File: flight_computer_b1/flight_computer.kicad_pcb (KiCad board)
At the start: 4 copper layers, 78 x 67 mm, 77 parts, among them J1 Pi Connector, J2 Conn_02x02_Odd_Even, J3 Conn_01x03, J4 DB25_Socket, J5 DB25_Socket, U1 IRLML6344TRPBF, U2 IRLML6344TRPBF, U3 IRLML6344TRPBF, U4 IRLML6344TRPBF, U5 LMR51430XDDCR, U6 ADS1158IRTCR, U7 MIC94161YCS-TR, U8 MCP6001-OT, U9 MCP6001-OT, Y1 32.768kHz

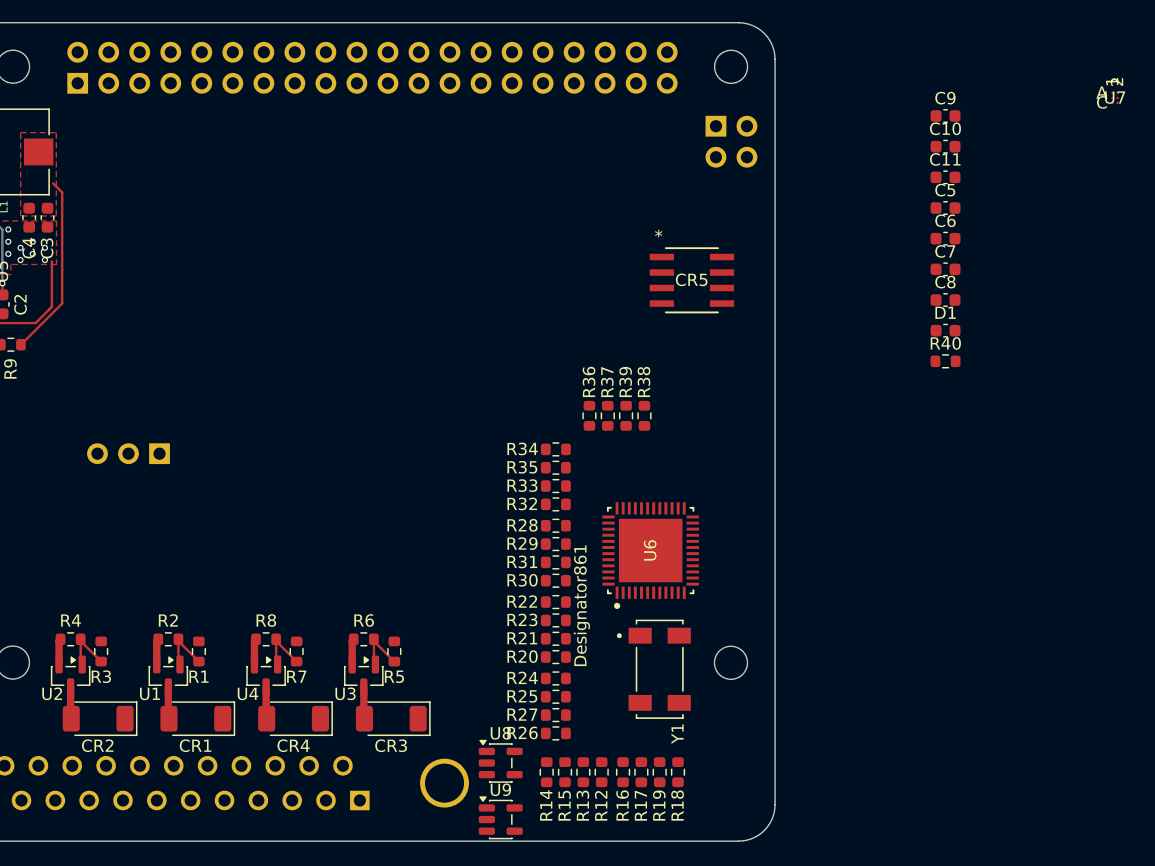
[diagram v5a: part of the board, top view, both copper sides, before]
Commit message: flight computer: added mux and voltage sense channels
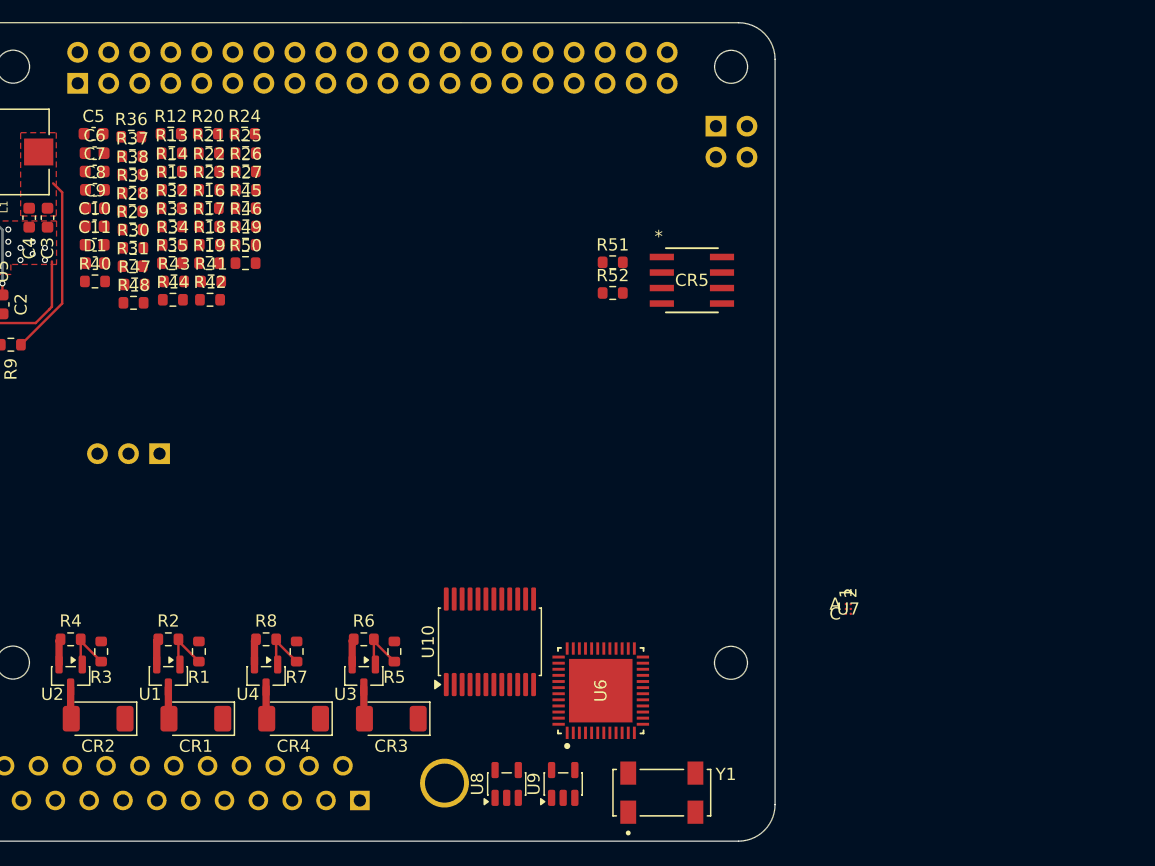
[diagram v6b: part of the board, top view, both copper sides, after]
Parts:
- added R41: 4k, Resistor_SMD:R_0603_1608Metric, F.Cu at (134.3, 92.5)
- added R42: 1k, Resistor_SMD:R_0603_1608Metric, F.Cu at (134.2, 94.0)
- added R43: 4k, Resistor_SMD:R_0603_1608Metric, F.Cu at (131.3, 92.5)
- added R44: 1k, Resistor_SMD:R_0603_1608Metric, F.Cu at (131.2, 94.0)
- added R45: 4k, Resistor_SMD:R_0603_1608Metric, F.Cu at (137.1, 86.5)
- added R46: 1k, Resistor_SMD:R_0603_1608Metric, F.Cu at (137.2, 88.0)
- added R47: 4k, Resistor_SMD:R_0603_1608Metric, F.Cu at (128.1, 92.8)
- added R48: 1k, Resistor_SMD:R_0603_1608Metric, F.Cu at (128.0, 94.3)
- added R49: 4k, Resistor_SMD:R_0603_1608Metric, F.Cu at (137.1, 89.5)
- added R50: 1k, Resistor_SMD:R_0603_1608Metric, F.Cu at (137.1, 91.0)
- added R51: 1k, Resistor_SMD:R_0603_1608Metric, F.Cu at (167.2, 90.9)
- added R52: 1k, Resistor_SMD:R_0603_1608Metric, F.Cu at (167.2, 93.5)
- added U10: CD74HC4067SM, Package_SO:SSOP-24_5.3x8.2mm_P0.65mm, F.Cu at (157.1, 122.0)
- moved C8 70.2 mm to (124.8, 85.0)
- moved C7 70.1 mm to (124.8, 83.5)
- moved C9 70.0 mm to (124.8, 86.5)
- moved C6 70.0 mm to (124.8, 82.0)
- moved C5 70.0 mm to (124.7, 80.4)
- moved C10 70.0 mm to (124.8, 88.0)
- moved R40 69.9 mm to (124.8, 92.5)
- moved C11 69.9 mm to (124.8, 89.5)
- moved D1 69.8 mm to (124.8, 91.0)
- moved R12 63.1 mm to (131.0, 80.4), turned to 0 degrees
- moved R13 60.9 mm to (131.1, 82.0), turned to 0 degrees
- moved R14 58.0 mm to (131.1, 83.5), turned to 0 degrees
- moved R18 57.7 mm to (134.2, 89.5), turned to 0 degrees
- moved R15 57.5 mm to (131.1, 85.0), turned to 0 degrees
- moved R16 57.3 mm to (134.1, 86.5), turned to 0 degrees
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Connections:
- net /pt_div0/INPUT+ renamed /PT_0+
- net /pt_div0/INPUT- renamed /PT_0-
- net /pt_div1/INPUT+ renamed /PT_1+
- net /pt_div1/INPUT- renamed /PT_1-
- net /pt_div2/INPUT+ renamed /PT_2+
- net /pt_div2/INPUT- renamed /PT_2-
- net /pt_div3/INPUT+ renamed /PT_3+
- net /pt_div3/INPUT- renamed /PT_3-
- net /pt_div4/INPUT+ renamed /PT_4+
- net /pt_div4/INPUT- renamed /PT_4-
- net /pt_div5/INPUT+ renamed /PT_5+
- net /pt_div5/INPUT- renamed /PT_5-
- net /pt_div6/INPUT+ renamed /PT_6+
- net /pt_div6/INPUT- renamed /PT_6-
- C3 pad 1: +5V -> /24_5_buck/5V
- C4 pad 1: +5V -> /24_5_buck/5V
- CR5 pad 1: +5V_ISO -> +5V
- J1 pad 2: +5V_ISO -> +5V
- J1 pad 29: unconnected-(J1-Pin_29-Pad29) -> /valve3_enable
- J1 pad 3: unconnected-(J1-Pin_3-Pad3) -> /valve0_enable
- J1 pad 4: +5V_ISO -> +5V
- J1 pad 5: unconnected-(J1-Pin_5-Pad5) -> /valve1_enable
- J1 pad 7: unconnected-(J1-Pin_7-Pad7) -> /valve2_enable
- L1 pad 2: +5V -> /24_5_buck/5V
- R1 pad 1: /valve0/ENABLE -> /valve0_enable
- R3 pad 1: /valve1/ENABLE -> /valve1_enable
- R5 pad 1: /valve2/ENABLE -> /valve2_enable
- R7 pad 1: /valve3/ENABLE -> /valve3_enable
- R9 pad 1: +5V -> /24_5_buck/5V
- U1 pad 1: Net-(U1-G) -> /valve0_excitation_return
- U1 pad 2: GND -> Net-(U1-G)
- U1 pad 3: /valve0_excitation_return -> GND
- U2 pad 1: Net-(U2-G) -> /valve1_excitation_return
- U2 pad 2: GND -> Net-(U2-G)
- U2 pad 3: /valve1_excitation_return -> GND
- U3 pad 1: Net-(U3-G) -> /valve2_excitation_return
- U3 pad 2: GND -> Net-(U3-G)
- U3 pad 3: /valve2_excitation_return -> GND
- U4 pad 1: Net-(U4-G) -> /valve3_excitation_return
- U4 pad 2: GND -> Net-(U4-G)
- U4 pad 3: /valve3_excitation_return -> GND
- U6 pad 10: +5V_ISO -> +5V
- U6 pad 11: +5V_ISO -> +5V
- U6 pad 26: +5V_ISO -> +5V
- U7 pad A1: +5V_ISO -> +5V
- U7 pad A2: +5V -> /24_5_buck/5V
- U7 pad B1: +5V_ISO -> +5V
- U7 pad B2: +5V -> /24_5_buck/5V
- U7 pad C2: +5V -> /24_5_buck/5V
- U8 pad 5: +5V_ISO -> +5V
- U9 pad 5: +5V_ISO -> +5V
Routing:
- net /24_5_buck/5V: track 0.00 -> 14.9 mm
- net +5V: track 14.9 -> 0.00 mm
- net Net-(U2-G): track 4.63 -> 0.00 mm
- net /valve1_excitation_return: track 2.58 -> 7.22 mm
- net Net-(U4-G): track 4.63 -> 0.00 mm
- net Net-(U3-G): track 4.63 -> 0.00 mm
- net /valve3_excitation_return: track 2.58 -> 7.22 mm
- net /valve2_excitation_return: track 2.58 -> 7.22 mm

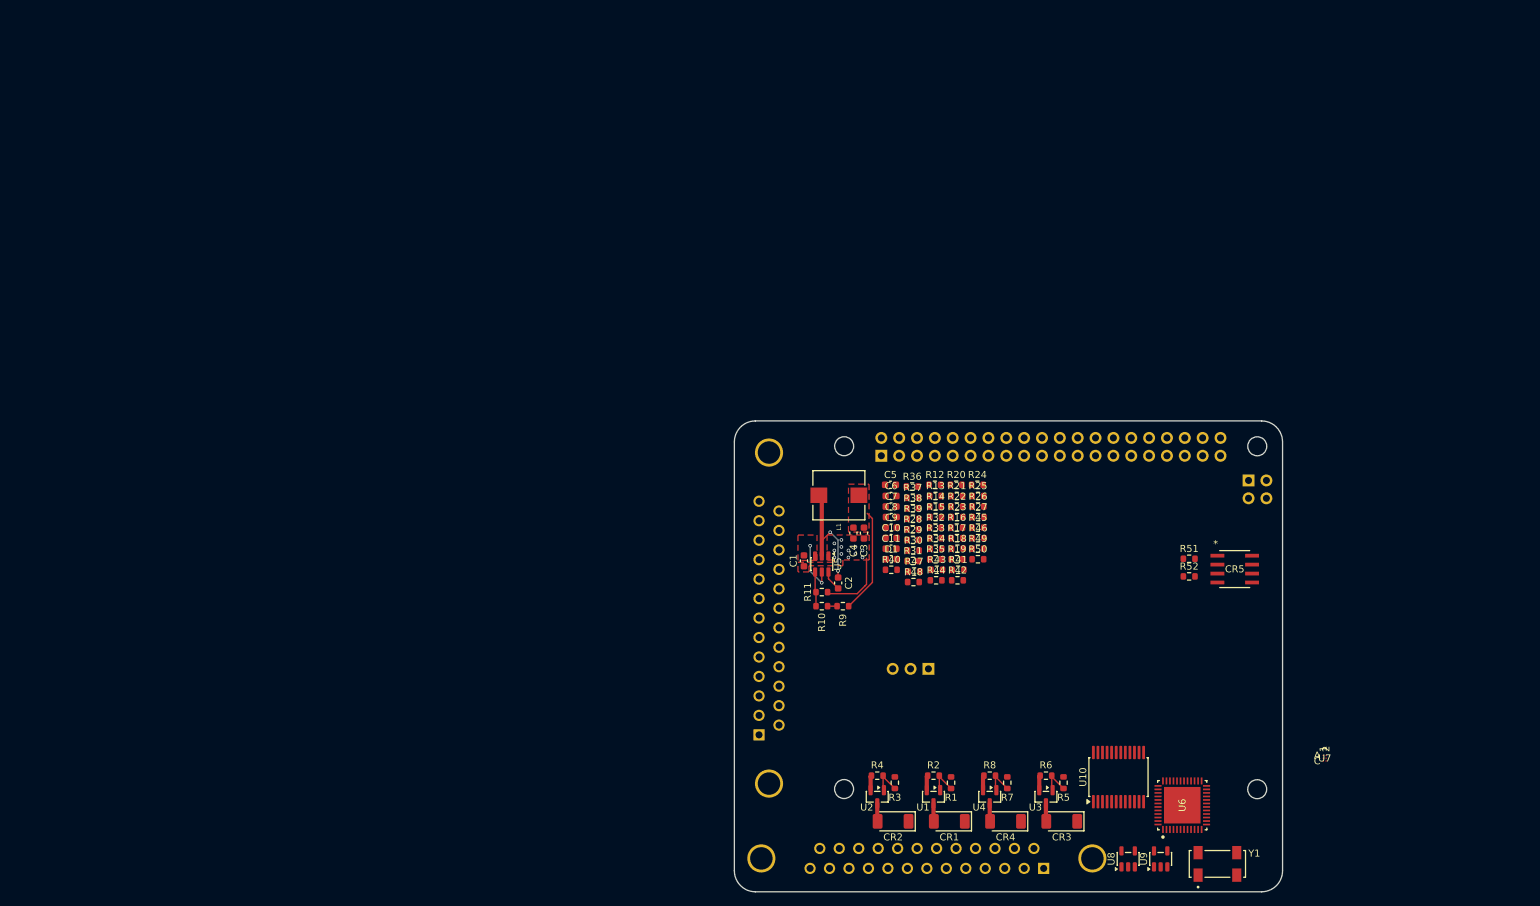
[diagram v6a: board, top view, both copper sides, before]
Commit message: flight computer: added pyro circuit and digikey part numbers
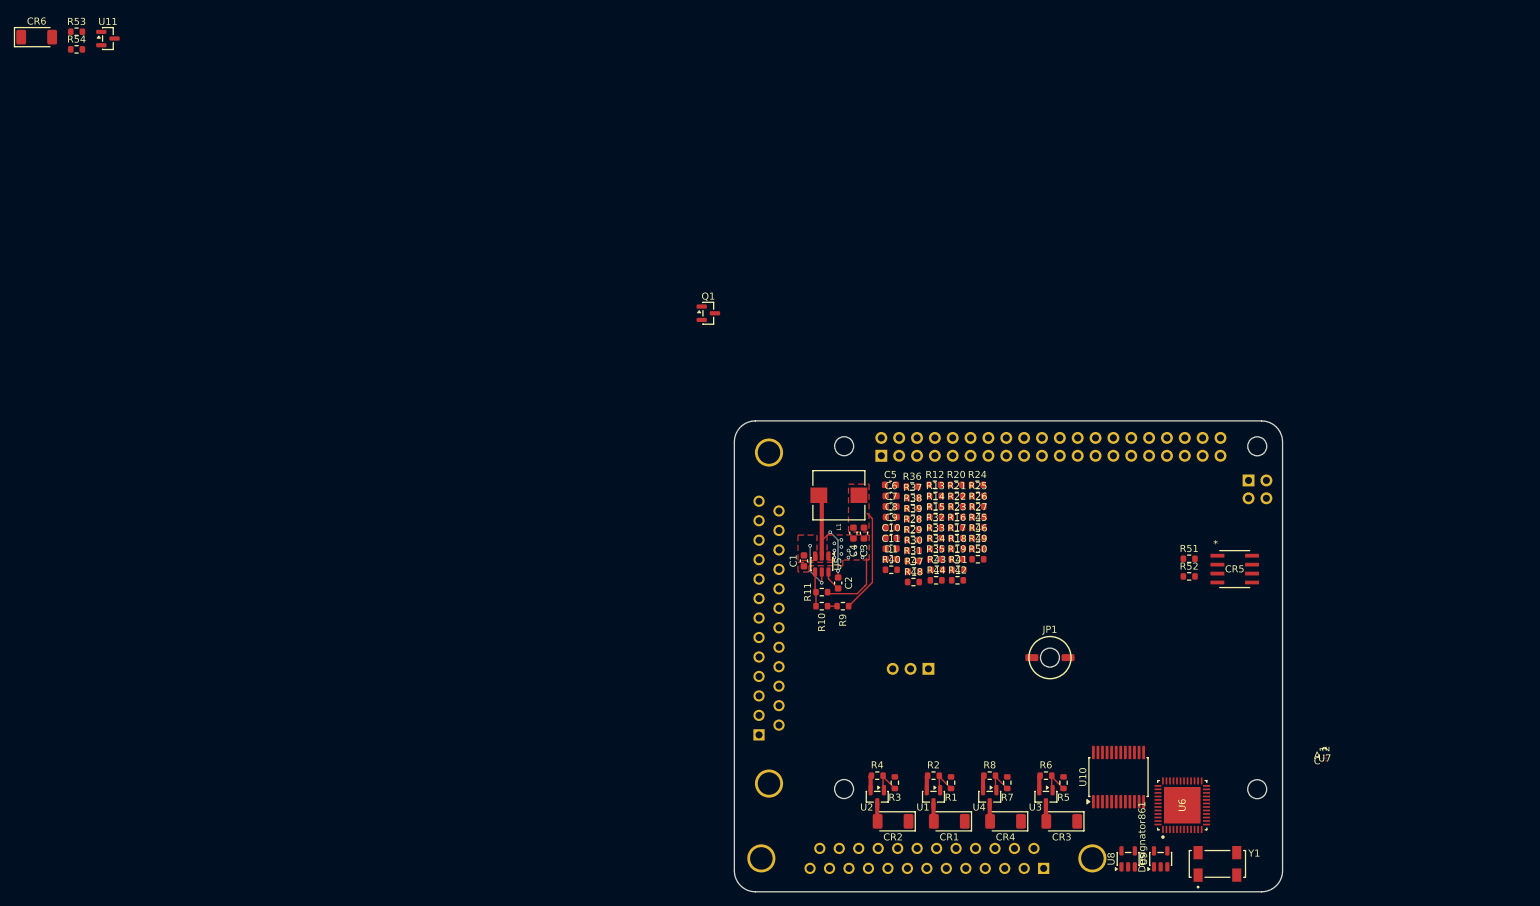
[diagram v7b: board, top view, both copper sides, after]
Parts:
- added CR6: STPS360AF, Diode_SMD:D_SOD-128, F.Cu at (3.22, 16.7)
- added JP1: SCREW_SHUNT, avi_lib:Screw_Shunt, F.Cu at (147.4, 105.0)
- added Q1: MMBT3904, Package_TO_SOT_SMD:SOT-23, F.Cu at (98.8, 56.0)
- added R53: 100, Resistor_SMD:R_0603_1608Metric, F.Cu at (8.89, 16.0)
- added R54: 1k, Resistor_SMD:R_0603_1608Metric, F.Cu at (8.89, 18.5)
- added U11: IRLML6344TRPBF, Package_TO_SOT_SMD:SOT-23, F.Cu at (13.4, 16.9)
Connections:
- J1 pad 16: unconnected-(J1-Pin_16-Pad16) -> /PYRO_FIRE
- J1 pad 18: unconnected-(J1-Pin_18-Pad18) -> /PYRO_ARM
- J1 pad 31: unconnected-(J1-Pin_31-Pad31) -> /mux_addr0
- J1 pad 33: unconnected-(J1-Pin_33-Pad33) -> /mux_addr1
- J1 pad 35: unconnected-(J1-Pin_35-Pad35) -> /mux_addr2
- J1 pad 37: unconnected-(J1-Pin_37-Pad37) -> /mux_addr3
- R49 pad 1: /pyro_excitation -> /pyro_excitation_return
- U10 pad 10: /mux0/select0 -> /mux_addr0
- U10 pad 11: /mux0/select1 -> /mux_addr1
- U10 pad 13: /mux0/select3 -> /mux_addr3
- U10 pad 14: /mux0/select2 -> /mux_addr2

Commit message: flight computer: new ideal diode, small schematic changes
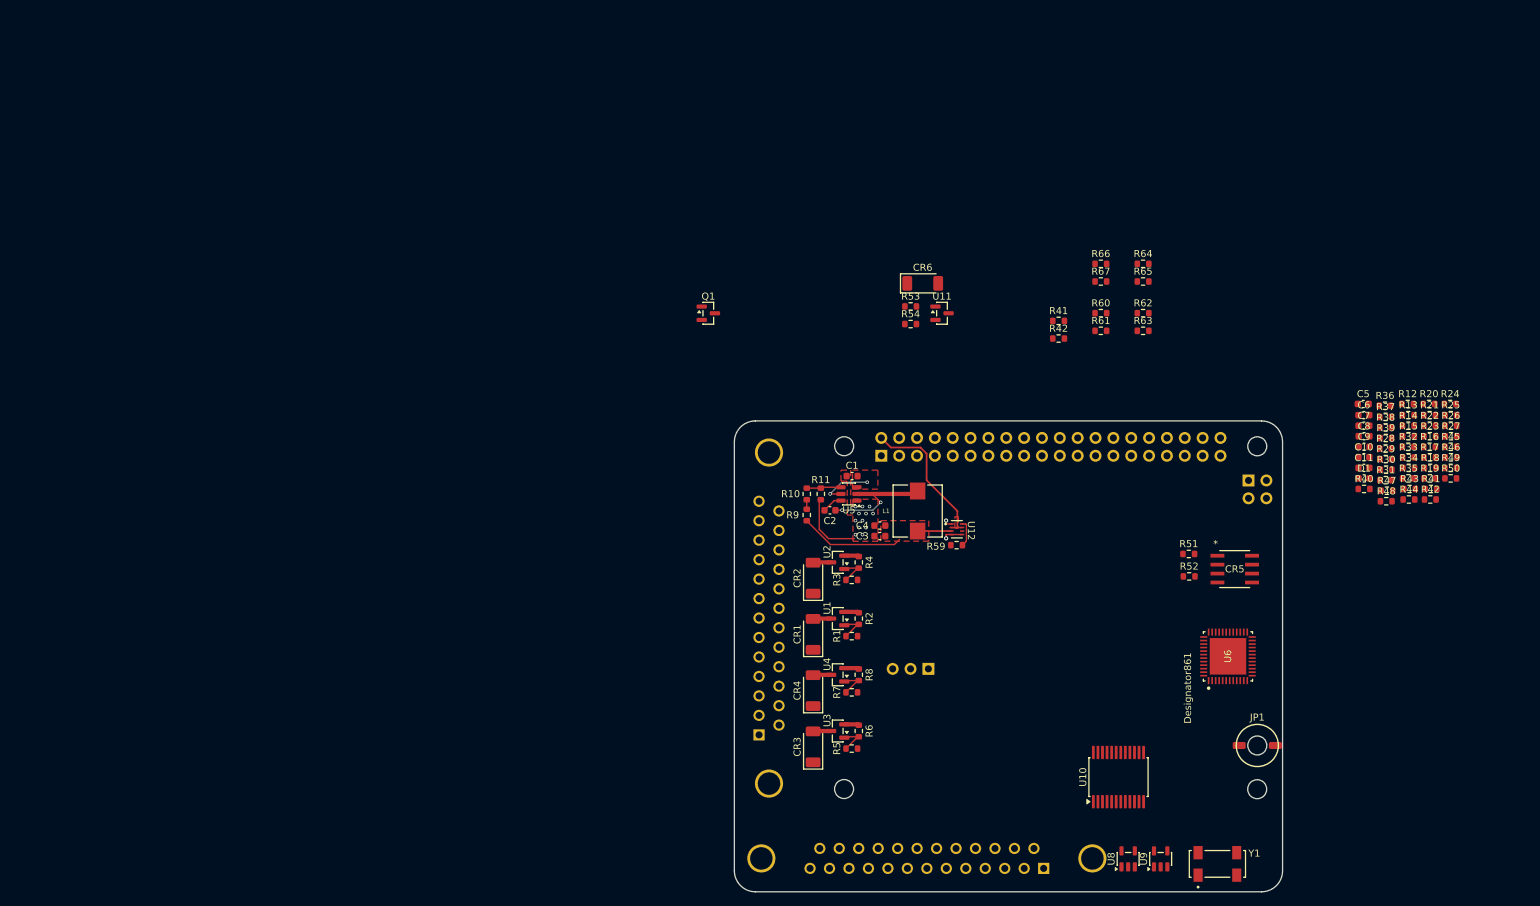
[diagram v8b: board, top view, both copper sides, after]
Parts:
- removed U7: MIC94161YCS-TR, avi_lib:MIC94161YCS_TR
- added R41: 4k, Resistor_SMD:R_0603_1608Metric, F.Cu at (148.6, 57.1)
- added R42: 1k, Resistor_SMD:R_0603_1608Metric, F.Cu at (148.6, 59.6)
- added R59: 1k, Resistor_SMD:R_0603_1608Metric, F.Cu at (134.1, 89.0)
- added R60: 4k, Resistor_SMD:R_0603_1608Metric, F.Cu at (154.6, 56.0)
- added R61: 1k, Resistor_SMD:R_0603_1608Metric, F.Cu at (154.6, 58.5)
- added R62: 4k, Resistor_SMD:R_0603_1608Metric, F.Cu at (160.6, 56.0)
- added R63: 1k, Resistor_SMD:R_0603_1608Metric, F.Cu at (160.6, 58.5)
- added R64: 4k, Resistor_SMD:R_0603_1608Metric, F.Cu at (160.6, 49.0)
- added R65: 1k, Resistor_SMD:R_0603_1608Metric, F.Cu at (160.6, 51.5)
- added R66: 4k, Resistor_SMD:R_0603_1608Metric, F.Cu at (154.6, 49.0)
- added R67: 1k, Resistor_SMD:R_0603_1608Metric, F.Cu at (154.6, 51.5)
- added U12: LM66200DRLR, avi_lib:SOT-5X3_DRL_TEX-L, F.Cu at (134.1, 86.7)
- moved CR6 130.8 mm to (129.3, 51.8)
- moved R53 124.9 mm to (127.6, 55.0)
- moved R54 124.9 mm to (127.6, 57.5)
- moved U11 124.9 mm to (132.0, 56.0)
- moved C6 68.3 mm to (192.1, 70.5)
- moved C8 68.3 mm to (192.1, 73.5)
- moved C9 68.3 mm to (192.1, 75.0)
- moved D1 68.3 mm to (192.1, 79.5)
- moved R12 68.3 mm to (198.3, 68.9)
- moved R13 68.3 mm to (198.4, 70.5)
- moved R14 68.3 mm to (198.4, 72.0)
- moved R15 68.3 mm to (198.4, 73.5)
- moved R16 68.3 mm to (201.4, 75.0)
- moved R17 68.3 mm to (201.4, 76.5)
- moved R18 68.3 mm to (201.5, 78.0)
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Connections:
- J4 pad 10: unconnected-(J4-Pad10) -> /PT_2-
- J4 pad 11: unconnected-(J4-Pad11) -> /PT_3+
- J4 pad 12: unconnected-(J4-Pad12) -> /PT_3-
- J4 pad 13: unconnected-(J4-Pad13) -> /PT_4+
- J4 pad 14: unconnected-(J4-P14-Pad14) -> /PT_4-
- J4 pad 15: unconnected-(J4-P15-Pad15) -> /pyro_excitation
- J4 pad 16: unconnected-(J4-P16-Pad16) -> /pyro_excitation_return
- J4 pad 17: unconnected-(J4-P17-Pad17) -> +24V
- J4 pad 18: unconnected-(J4-P18-Pad18) -> /valve0_excitation_return
- J4 pad 19: unconnected-(J4-P19-Pad19) -> +24V
- J4 pad 20: unconnected-(J4-P20-Pad20) -> /valve1_excitation_return
- J4 pad 3: unconnected-(J4-Pad3) -> /PT_0+
- J4 pad 4: unconnected-(J4-Pad4) -> /PT_0-
- J4 pad 7: unconnected-(J4-Pad7) -> /PT_1+
- J4 pad 8: unconnected-(J4-Pad8) -> /PT_1-
- J4 pad 9: unconnected-(J4-Pad9) -> /PT_2+
- U11 pad 1: Net-(U11-D) -> Net-(JP1-A)
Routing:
- net +5V: track 0.00 -> 21.2 mm
- net /24_5_buck/5V: track 14.9 -> 19.7 mm
- net GND: track 18.4 -> 22.4 mm, vias 12 -> 14
- net Net-(U12-ST): track 0.00 -> 3.80 mm
- added copper zone on F.Cu, net /24_5_buck/5V
